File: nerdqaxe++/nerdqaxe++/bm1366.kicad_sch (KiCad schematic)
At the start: 78 parts, among them J2 Conn_01x06, U19 BM1370_mode1, U20 BM1370_mode1, U25 BM1370_mode1, U26 BM1370_mode1, U35 TXU0304PW, U8 25MHz

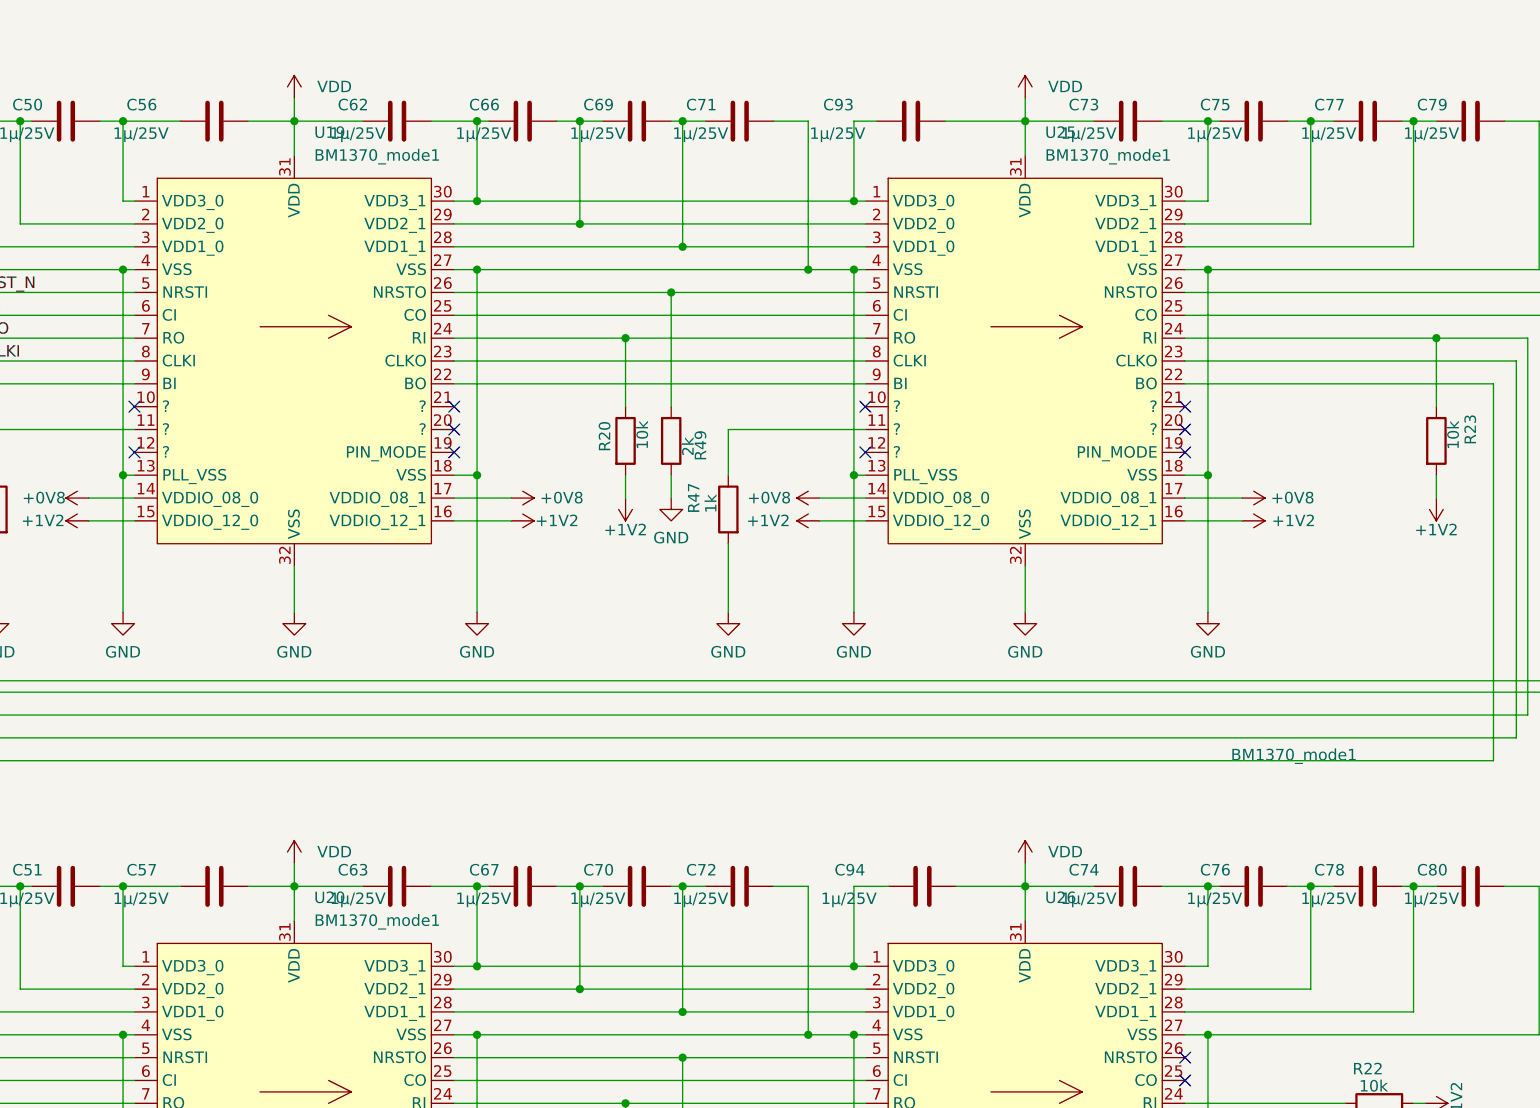
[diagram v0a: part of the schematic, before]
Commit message: Nerdqaxe++ rev6.1.2PM
1. BM1370 Footprint solder paste revision
2. Added 2R2 resistor in series with bootstrap cap for CSD95472Q5MC
3. 180nH inductors for CSD
4. Vsense closer to ASICs
5. Fiducials
6. Updated top silkscreen
7. Various changes in tracing
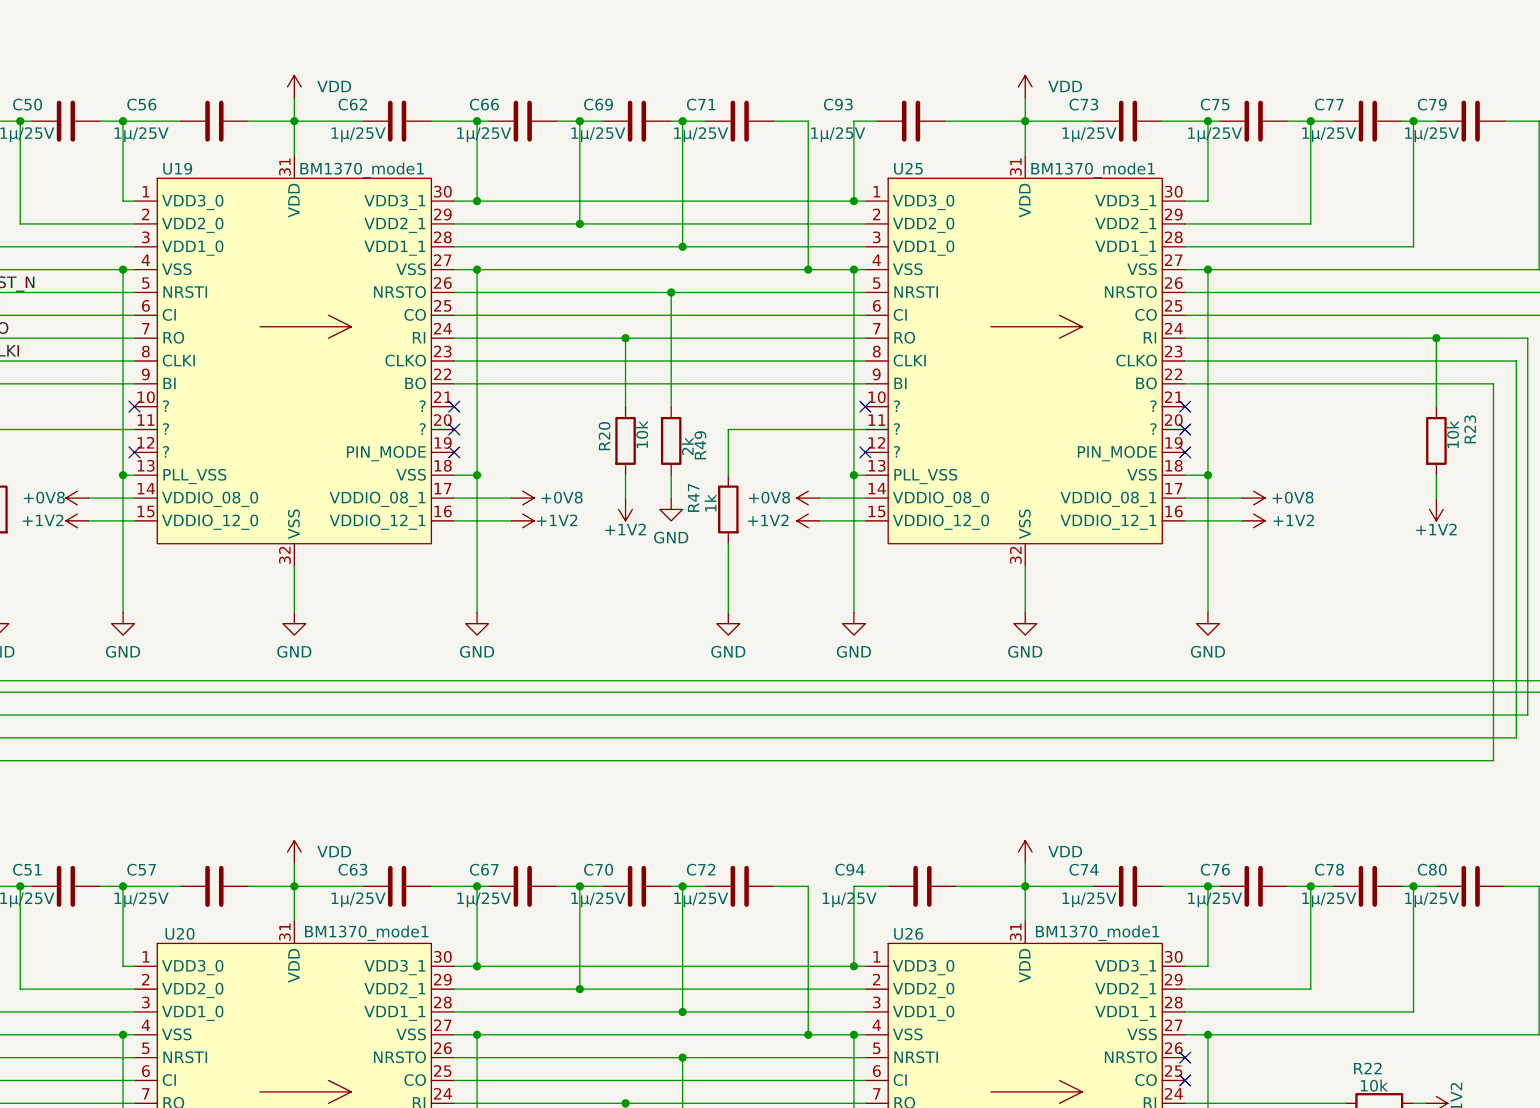
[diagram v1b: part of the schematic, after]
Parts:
- U19, U20, U25, U26: footprint myfootprints:BM1370 -> qaxe:BM1370_JB
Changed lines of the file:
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@@
 		(on_board yes)
 		(dnp no)
-		(fields_autoplaced yes)
 		(property "Reference" "U25"
-			(at 219.3641 43.18 0)
+			(at 202.438 47.244 0)
 			(effects
 				(font
@@
 		)
 		(property "Value" "BM1370_mode1"
-			(at 219.3641 45.72 0)
+			(at 217.678 47.244 0)
 			(effects
 				(font
@@
 			)
 		)
-		(property "Footprint" "myfootprints:BM1370"
+		(property "Footprint" "qaxe:BM1370_JB"
 			(at 233.68 101.6 0)
 			(effects
@@
 		(dnp no)
 		(property "Reference" "U26"
-			(at 219.3641 128.27 0)
+			(at 202.438 132.334 0)
 			(effects
 				(font
@@
 		)
 		(property "Value" "BM1370_mode1"
-			(at 240.03 112.395 0)
+			(at 218.186 132.08 0)
 			(effects
 				(font
@@
 			)
 		)
-		(property "Footprint" "myfootprints:BM1370"
+		(property "Footprint" "qaxe:BM1370_JB"
 			(at 233.68 186.69 0)
 			(effects
@@
 		(on_board yes)
 		(dnp no)
-		(fields_autoplaced yes)
 		(property "Reference" "U19"
-			(at 138.0841 43.18 0)
+			(at 121.158 47.244 0)
 			(effects
 				(font
@@
 		)
 		(property "Value" "BM1370_mode1"
-			(at 138.0841 45.72 0)
+			(at 136.398 47.244 0)
 			(effects
 				(font
@@
 			)
 		)
-		(property "Footprint" "myfootprints:BM1370"
+		(property "Footprint" "qaxe:BM1370_JB"
 			(at 152.4 101.6 0)
 			(effects
@@
 		(on_board yes)
 		(dnp no)
-		(fields_autoplaced yes)
 		(property "Reference" "U20"
-			(at 138.0841 128.27 0)
+			(at 121.412 132.334 0)
 			(effects
 				(font
@@
 		)
 		(property "Value" "BM1370_mode1"
-			(at 138.0841 130.81 0)
+			(at 136.906 132.08 0)
 			(effects
 				(font
@@
 			)
 		)
-		(property "Footprint" "myfootprints:BM1370"
+		(property "Footprint" "qaxe:BM1370_JB"
 			(at 152.4 186.69 0)
 			(effects
